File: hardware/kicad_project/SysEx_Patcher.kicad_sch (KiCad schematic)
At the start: 89 parts, among them J1 MIDI_IN, J10 JACK6.35, J2 MIDI_OUT, J3 DC_5V, J4 BAT_PWR, J5 OLED, SW2 SW, SW3 SW, SW4 SW, SW5 SW, SW6 SW, SW7 SW, SW8 SW, U1 6N138, U2 CD74HC4067

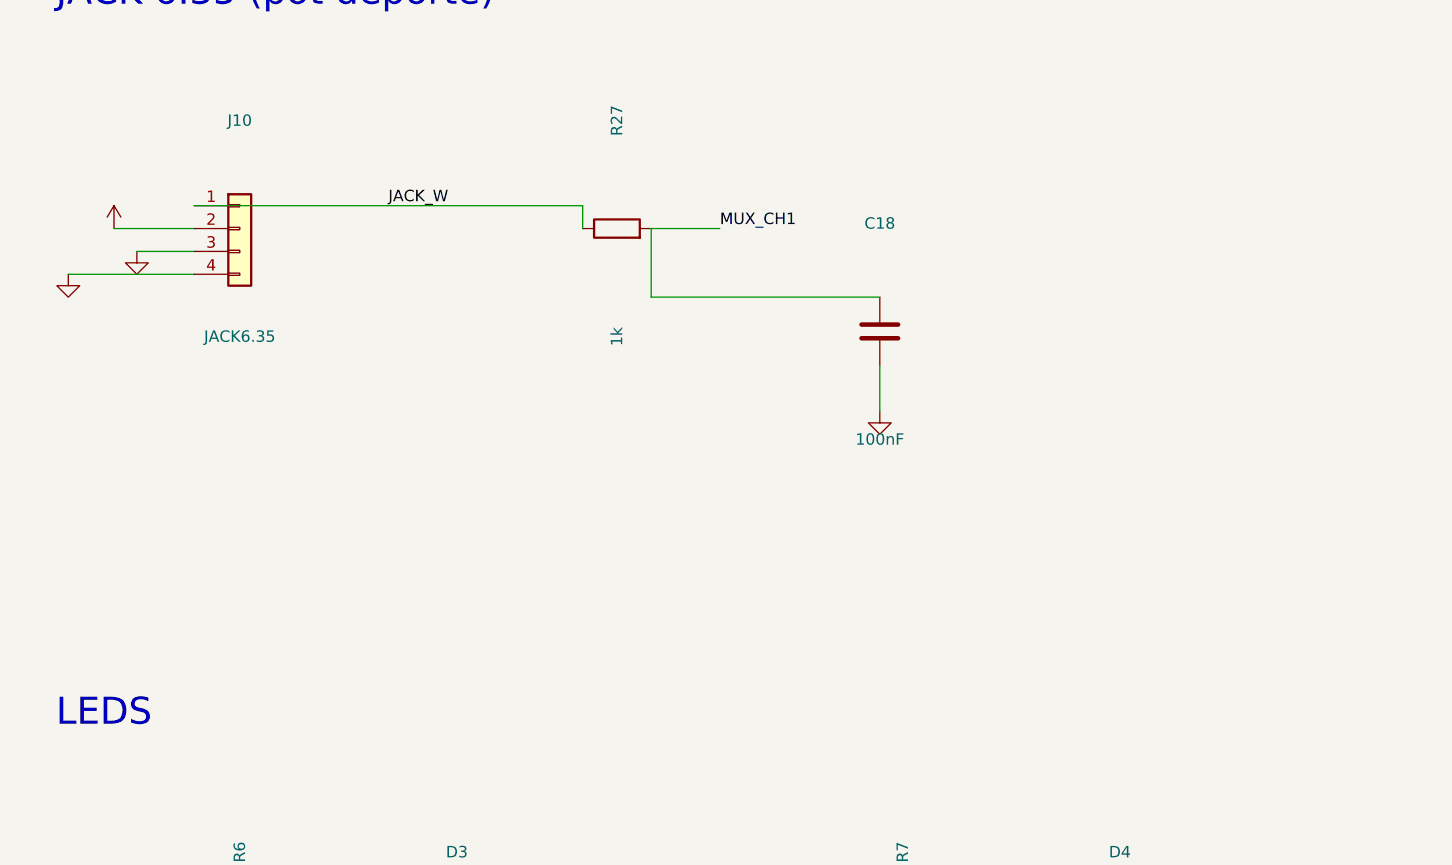
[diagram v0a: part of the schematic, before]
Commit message: schéma v1.1: J10 en mini-XLR 5 points + filtre RC et pull-down du canal switch
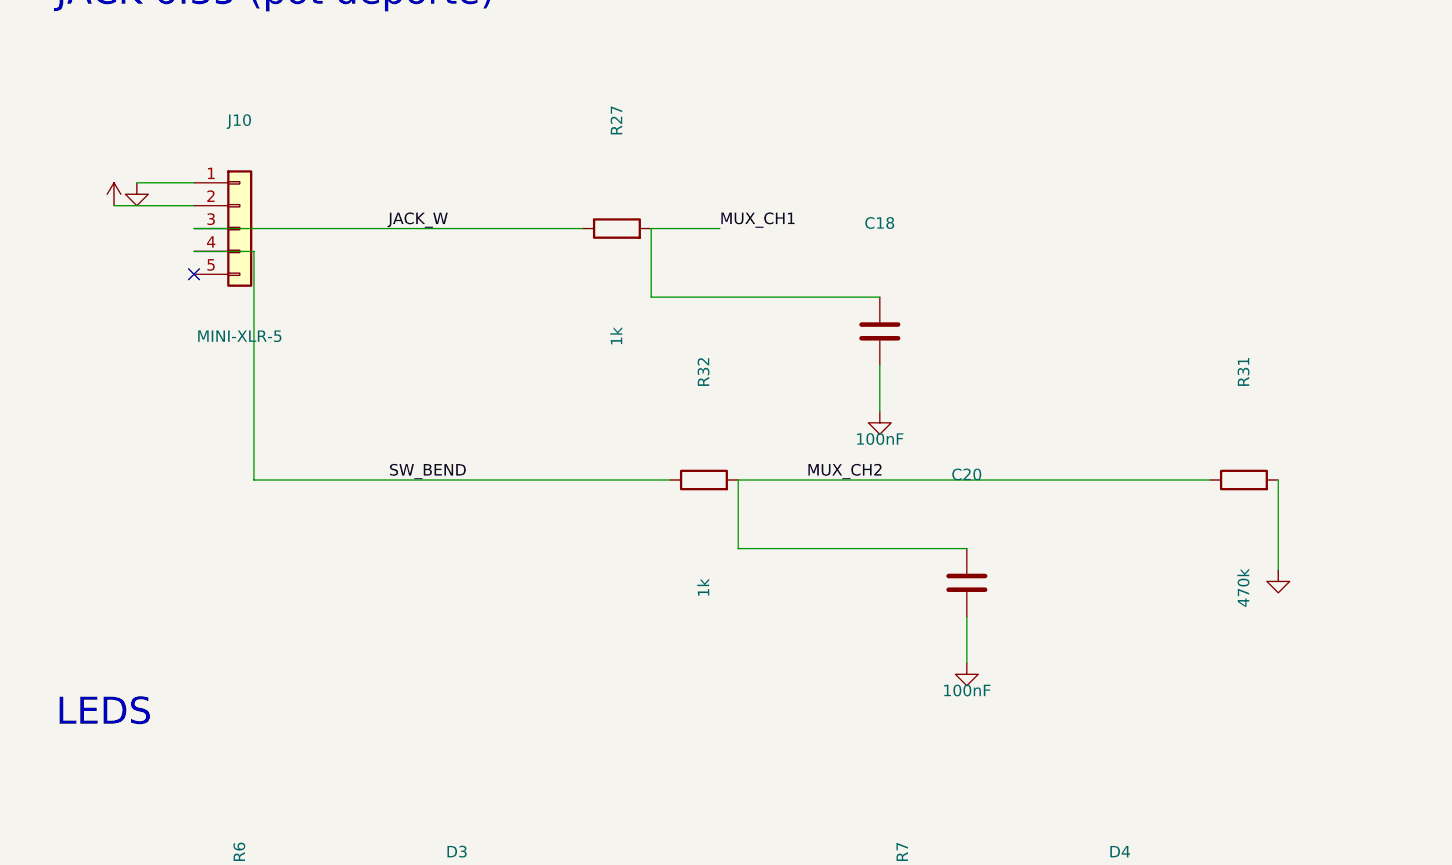
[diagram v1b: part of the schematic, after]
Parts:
- added C20: 100nF, Capacitor_THT:C_Disc_D5.0mm_W2.5mm_P5.00mm, symbol Device:C
- added R31: 470k, Resistor_THT:R_Axial_DIN0207_L6.3mm_D2.5mm_P10.16mm_Horizontal, symbol Device:R
- added R32: 1k, Resistor_THT:R_Axial_DIN0207_L6.3mm_D2.5mm_P10.16mm_Horizontal, symbol Device:R
- J10: value JACK6.35 -> MINI-XLR-5; footprint Connector_Audio:Jack_6.35mm_Neutrik_NRJ6HF-1_Horizontal -> Connector_Audio:MiniXLR-5_Switchcraft_TRAPC_Horizontal; symbol Connector_Generic:Conn_01x04 -> Connector_Generic:Conn_01x05
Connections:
- net GND: now also J10.1 (Pin_1), C20.2, R31.2; no longer J10.3 (Pin_3), J10.4 (Pin_4)
- net JACK_W: now also J10.3 (Pin_3); no longer J10.1 (Pin_1)
- net MUX_CH2: now also C20.1, R31.1, R32.2
- new net SW_BEND: J10.4 (Pin_4), R32.1
- no-connect marks 6 -> 7
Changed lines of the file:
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@@
   (property "Footprint" "Resistor_THT:R_Axial_DIN0207_L6.3mm_D2.5mm_P10.16mm_Horizontal" (at 308.61 132.08 0)(effects (font (size 1.27 1.27)) hide))
   (instances (project "SysEx_Patcher" (path "/" (reference "R3")(unit 1)))))
-(symbol (lib_id "Connector_Generic:Conn_01x04")(at 58.42 198.12 0)(unit 1)
+(symbol (lib_id "Connector_Generic:Conn_01x05")(at 58.42 198.12 0)(unit 1)
   (exclude_from_sim no)(in_bom yes)(on_board yes)(dnp no)
   (property "Reference" "J10" (at 58.42 186.12 0)(effects (font (size 1.27 1.27))))
-  (property "Value" "JACK6.35" (at 58.42 210.12 0)(effects (font (size 1.27 1.27))))
-  (property "Footprint" "Connector_Audio:Jack_6.35mm_Neutrik_NRJ6HF-1_Horizontal" (at 58.42 198.12 0)(effects (font (size 1.27 1.27)) hide))
+  (property "Value" "MINI-XLR-5" (at 58.42 210.12 0)(effects (font (size 1.27 1.27))))
+  (property "Footprint" "Connector_Audio:MiniXLR-5_Switchcraft_TRAPC_Horizontal" (at 58.42 198.12 0)(effects (font (size 1.27 1.27)) hide))
   (instances (project "SysEx_Patcher" (path "/" (reference "J10")(unit 1)))))
-(symbol (lib_id "power:+5V")(at 44.45 198.12 0)(unit 1)
-  (exclude_from_sim no)(in_bom yes)(on_board yes)(dnp no)
-  (property "Reference" "#PWR20" (at 44.45 186.12 0)(effects (font (size 1.27 1.27)) hide))
-  (property "Value" "+5V" (at 44.45 210.12 0)(effects (font (size 1.27 1.27)) hide))
-  (property "Footprint" "" (at 44.45 198.12 0)(effects (font (size 1.27 1.27)) hide))
+(symbol (lib_id "power:+5V")(at 44.45 195.58 0)(unit 1)
+  (exclude_from_sim no)(in_bom yes)(on_board yes)(dnp no)
+  (property "Reference" "#PWR20" (at 44.45 183.58 0)(effects (font (size 1.27 1.27)) hide))
+  (property "Value" "+5V" (at 44.45 207.58 0)(effects (font (size 1.27 1.27)) hide))
+  (property "Footprint" "" (at 44.45 195.58 0)(effects (font (size 1.27 1.27)) hide))
   (instances (project "SysEx_Patcher" (path "/" (reference "#PWR20")(unit 1)))))
-(symbol (lib_id "power:GND")(at 46.99 200.66 0)(unit 1)
-  (exclude_from_sim no)(in_bom yes)(on_board yes)(dnp no)
-  (property "Reference" "#PWR21" (at 46.99 188.66 0)(effects (font (size 1.27 1.27)) hide))
-  (property "Value" "GND" (at 46.99 212.66 0)(effects (font (size 1.27 1.27)) hide))
-  (property "Footprint" "" (at 46.99 200.66 0)(effects (font (size 1.27 1.27)) hide))
+(symbol (lib_id "power:GND")(at 46.99 193.04 0)(unit 1)
+  (exclude_from_sim no)(in_bom yes)(on_board yes)(dnp no)
+  (property "Reference" "#PWR21" (at 46.99 181.04 0)(effects (font (size 1.27 1.27)) hide))
+  (property "Value" "GND" (at 46.99 205.04 0)(effects (font (size 1.27 1.27)) hide))
+  (property "Footprint" "" (at 46.99 193.04 0)(effects (font (size 1.27 1.27)) hide))
   (instances (project "SysEx_Patcher" (path "/" (reference "#PWR21")(unit 1)))))
-(symbol (lib_id "power:GND")(at 39.37 203.20 0)(unit 1)
-  (exclude_from_sim no)(in_bom yes)(on_board yes)(dnp no)
-  (property "Reference" "#PWR22" (at 39.37 191.20 0)(effects (font (size 1.27 1.27)) hide))
-  (property "Value" "GND" (at 39.37 215.20 0)(effects (font (size 1.27 1.27)) hide))
-  (property "Footprint" "" (at 39.37 203.20 0)(effects (font (size 1.27 1.27)) hide))
-  (instances (project "SysEx_Patcher" (path "/" (reference "#PWR22")(unit 1)))))
 (symbol (lib_id "Device:R")(at 100.33 198.12 90)(unit 1)
   (exclude_from_sim no)(in_bom yes)(on_board yes)(dnp no)
@@
   (property "Footprint" "" (at 129.54 218.44 0)(effects (font (size 1.27 1.27)) hide))
   (instances (project "SysEx_Patcher" (path "/" (reference "#PWR23")(unit 1)))))
+(symbol (lib_id "Device:R")(at 110.00 226.06 90)(unit 1)
+  (exclude_from_sim no)(in_bom yes)(on_board yes)(dnp no)
+  (property "Reference" "R32" (at 110.00 214.06 0)(effects (font (size 1.27 1.27))))
+  (property "Value" "1k" (at 110.00 238.06 0)(effects (font (size 1.27 1.27))))
+  (property "Footprint" "Resistor_THT:R_Axial_DIN0207_L6.3mm_D2.5mm_P10.16mm_Horizontal" (at 110.00 226.06 0)(effects (font (size 1.27 1.27)) hide))
+  (instances (project "SysEx_Patcher" (path "/" (reference "R32")(unit 1)))))
+(symbol (lib_id "Device:C")(at 139.21 237.49 0)(unit 1)
+  (exclude_from_sim no)(in_bom yes)(on_board yes)(dnp no)
+  (property "Reference" "C20" (at 139.21 225.49 0)(effects (font (size 1.27 1.27))))
+  (property "Value" "100nF" (at 139.21 249.49 0)(effects (font (size 1.27 1.27))))
+  (property "Footprint" "Capacitor_THT:C_Disc_D5.0mm_W2.5mm_P5.00mm" (at 139.21 237.49 0)(effects (font (size 1.27 1.27)) hide))
+  (instances (project "SysEx_Patcher" (path "/" (reference "C20")(unit 1)))))
+(symbol (lib_id "power:GND")(at 139.21 246.38 0)(unit 1)
+  (exclude_from_sim no)(in_bom yes)(on_board yes)(dnp no)
+  (property "Reference" "#PWR93" (at 139.21 234.38 0)(effects (font (size 1.27 1.27)) hide))
+  (property "Value" "GND" (at 139.21 258.38 0)(effects (font (size 1.27 1.27)) hide))
+  (property "Footprint" "" (at 139.21 246.38 0)(effects (font (size 1.27 1.27)) hide))
+  (instances (project "SysEx_Patcher" (path "/" (reference "#PWR93")(unit 1)))))
+(symbol (lib_id "Device:R")(at 170.00 226.06 90)(unit 1)
+  (exclude_from_sim no)(in_bom yes)(on_board yes)(dnp no)
+  (property "Reference" "R31" (at 170.00 214.06 0)(effects (font (size 1.27 1.27))))
+  (property "Value" "470k" (at 170.00 238.06 0)(effects (font (size 1.27 1.27))))
+  (property "Footprint" "Resistor_THT:R_Axial_DIN0207_L6.3mm_D2.5mm_P10.16mm_Horizontal" (at 170.00 226.06 0)(effects (font (size 1.27 1.27)) hide))
+  (instances (project "SysEx_Patcher" (path "/" (reference "R31")(unit 1)))))
+(symbol (lib_id "power:GND")(at 173.81 236.06 0)(unit 1)
+  (exclude_from_sim no)(in_bom yes)(on_board yes)(dnp no)
+  (property "Reference" "#PWR94" (at 173.81 224.06 0)(effects (font (size 1.27 1.27)) hide))
+  (property "Value" "GND" (at 173.81 248.06 0)(effects (font (size 1.27 1.27)) hide))
+  (property "Footprint" "" (at 173.81 236.06 0)(effects (font (size 1.27 1.27)) hide))
+  (instances (project "SysEx_Patcher" (path "/" (reference "#PWR94")(unit 1)))))
 (symbol (lib_id "Switch:SW_Push")(at 271.78 199.39 0)(unit 1)
   (exclude_from_sim no)(in_bom yes)(on_board yes)(dnp no)
@@
 (wire (pts (xy 304.80 121.92)(xy 304.80 132.08))(stroke (width 0)(type default)))
 (wire (pts (xy 312.42 132.08)(xy 320.04 132.08))(stroke (width 0)(type default)))
-(wire (pts (xy 53.34 198.12)(xy 44.45 198.12))(stroke (width 0)(type default)))
-(wire (pts (xy 53.34 200.66)(xy 46.99 200.66))(stroke (width 0)(type default)))
-(wire (pts (xy 53.34 203.20)(xy 39.37 203.20))(stroke (width 0)(type default)))
-(wire (pts (xy 53.34 195.58)(xy 96.52 195.58))(stroke (width 0)(type default)))
-(wire (pts (xy 96.52 195.58)(xy 96.52 198.12))(stroke (width 0)(type default)))
+(wire (pts (xy 53.34 193.04)(xy 46.99 193.04))(stroke (width 0)(type default)))
+(wire (pts (xy 53.34 195.58)(xy 44.45 195.58))(stroke (width 0)(type default)))
+(wire (pts (xy 53.34 198.12)(xy 96.52 198.12))(stroke (width 0)(type default)))
+(wire (pts (xy 53.34 200.66)(xy 60.00 200.66))(stroke (width 0)(type default)))
+(wire (pts (xy 60.00 200.66)(xy 60.00 226.06))(stroke (width 0)(type default)))
+(wire (pts (xy 60.00 226.06)(xy 106.19 226.06))(stroke (width 0)(type default)))
+(wire (pts (xy 113.81 226.06)(xy 166.19 226.06))(stroke (width 0)(type default)))
+(wire (pts (xy 113.81 226.06)(xy 113.81 233.68))(stroke (width 0)(type default)))
+(wire (pts (xy 113.81 233.68)(xy 139.21 233.68))(stroke (width 0)(type default)))
+(wire (pts (xy 139.21 241.30)(xy 139.21 246.38))(stroke (width 0)(type default)))
+(wire (pts (xy 173.81 226.06)(xy 173.81 236.06))(stroke (width 0)(type default)))
 (wire (pts (xy 104.14 198.12)(xy 104.14 205.74))(stroke (width 0)(type default)))
 (wire (pts (xy 104.14 205.74)(xy 129.54 205.74))(stroke (width 0)(type default)))
@@
 (label "MIDI_OUT_5" (at 290.83 121.92 0)(effects (font (size 1.27 1.27))(justify left bottom)))
 (label "D1_TX" (at 320.04 132.08 0)(effects (font (size 1.27 1.27))(justify left bottom)))
-(label "JACK_W" (at 74.93 195.58 0)(effects (font (size 1.27 1.27))(justify left bottom)))
+(label "JACK_W" (at 74.93 198.12 0)(effects (font (size 1.27 1.27))(justify left bottom)))
 (label "MUX_CH1" (at 111.76 198.12 0)(effects (font (size 1.27 1.27))(justify left bottom)))
+(label "SW_BEND" (at 75.00 226.06 0)(effects (font (size 1.27 1.27))(justify left bottom)))
+(label "MUX_CH2" (at 121.43 226.06 0)(effects (font (size 1.27 1.27))(justify left bottom)))
+(no_connect (at 53.34 203.20))
 (label "D7" (at 260.35 199.39 0)(effects (font (size 1.27 1.27))(justify right bottom)))
 (label "D8" (at 300.99 199.39 0)(effects (font (size 1.27 1.27))(justify right bottom)))

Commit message: pcb v1.2 : corrige l'emboîtement sur le Mega, supprime le 2×18
La v1.1 ne s'enfichait pas. Le placement des connecteurs venait du gabarit
Arduino_Mega livré avec KiCad, et ce gabarit est FAUX sur deux blocs : il place
le bloc de 10 broches 5,08 mm trop à gauche et le 2×18 17,78 mm trop à droite.
Un script maison annonçait pourtant « err_max = 0.00 mm » — il vérifiait
fidèlement la mauvaise référence.

Détecté en comparant à la carte de baritonomarchetto, fabriquée et qui s'enfiche
réellement, puis confirmé sur un modèle de Mega 2560 Rev3 réel. Les deux sources
concordent à 0,25 mm près, écart absorbé par le jeu des broches dans les trous.

CORRECTIONS
- JMD1 décalé de +5,080 mm
- JMX1 (2×18) supprimé : sa position réelle traverse la colonne de
  potentiomètres RV3/RV7/RV11/RV15, avec courts-circuits sur leur +5 V
- ses 6 signaux utiles (3 boutons, 3 LEDs) reportés sur D14-D19, libres sur
  JMD3. Les 26 autres broches n'avaient jamais rien porté.

La carte garde ses 7 boutons et 7 LEDs, 5 paires à droite et 2 à gauche, ce qui
correspond au besoin : 5 pages en accès direct plus dump et presets.

check_mega_fit.py remplace check_headers_world.py et valide contre
mega2560_reel.json, extrait d'un Mega réel. Les 6 connecteurs sont désormais à
0,000 mm de leur position attendue.

Routage complet, 0 connexion manquante. Subsistent 2 effleurements d'isolation
à 0,1995 mm contre 0,2000 requis — l'artefact d'arrondi déjà documenté.
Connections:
- net D22 renamed D14
- net D23 renamed D15
- net D24 renamed D16
- net D25 renamed D17
- net D26 renamed D18
- net D27 renamed D19
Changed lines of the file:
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@@
 (label "POT16_W" (at 632.46 410.21 0)(effects (font (size 1.27 1.27))(justify left bottom)))
 (label "MUX_CH0" (at 651.51 410.21 0)(effects (font (size 1.27 1.27))(justify left bottom)))
-(label "D22" (at 64.76 460.00 0)(effects (font (size 1.27 1.27))(justify right bottom)))
-(label "D24" (at 124.76 460.00 0)(effects (font (size 1.27 1.27))(justify right bottom)))
-(label "D26" (at 184.76 460.00 0)(effects (font (size 1.27 1.27))(justify right bottom)))
-(label "D23" (at 69.84 490.00 0)(effects (font (size 1.27 1.27))(justify right bottom)))
-(label "D25" (at 149.84 490.00 0)(effects (font (size 1.27 1.27))(justify right bottom)))
-(label "D27" (at 229.84 490.00 0)(effects (font (size 1.27 1.27))(justify right bottom)))
-(label "D22" (at 744.22 113.03 0)(effects (font (size 1.27 1.27))(justify left bottom)))
-(label "D23" (at 744.22 115.57 0)(effects (font (size 1.27 1.27))(justify left bottom)))
-(label "D24" (at 744.22 118.11 0)(effects (font (size 1.27 1.27))(justify left bottom)))
-(label "D25" (at 744.22 120.65 0)(effects (font (size 1.27 1.27))(justify left bottom)))
-(label "D26" (at 744.22 123.19 0)(effects (font (size 1.27 1.27))(justify left bottom)))
-(label "D27" (at 744.22 125.73 0)(effects (font (size 1.27 1.27))(justify left bottom)))
+(label "D14" (at 64.76 460.00 0)(effects (font (size 1.27 1.27))(justify right bottom)))
+(label "D16" (at 124.76 460.00 0)(effects (font (size 1.27 1.27))(justify right bottom)))
+(label "D18" (at 184.76 460.00 0)(effects (font (size 1.27 1.27))(justify right bottom)))
+(label "D15" (at 69.84 490.00 0)(effects (font (size 1.27 1.27))(justify right bottom)))
+(label "D17" (at 149.84 490.00 0)(effects (font (size 1.27 1.27))(justify right bottom)))
+(label "D19" (at 229.84 490.00 0)(effects (font (size 1.27 1.27))(justify right bottom)))
+(label "D14" (at 744.22 113.03 0)(effects (font (size 1.27 1.27))(justify left bottom)))
+(label "D15" (at 744.22 115.57 0)(effects (font (size 1.27 1.27))(justify left bottom)))
+(label "D16" (at 744.22 118.11 0)(effects (font (size 1.27 1.27))(justify left bottom)))
+(label "D17" (at 744.22 120.65 0)(effects (font (size 1.27 1.27))(justify left bottom)))
+(label "D18" (at 744.22 123.19 0)(effects (font (size 1.27 1.27))(justify left bottom)))
+(label "D19" (at 744.22 125.73 0)(effects (font (size 1.27 1.27))(justify left bottom)))
 (no_connect (at 50.80 123.19))
 (no_connect (at 58.42 113.03))
